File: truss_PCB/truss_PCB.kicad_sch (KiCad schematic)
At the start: 8 parts, among them J1 XT60_60A_male, J2 LimitSwitch, J3 Servo, J4 Truss Connection

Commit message: updating truss PCB
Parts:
- J3: symbol Connector:Conn_01x03_Male -> Connector:Conn_01x01_Male
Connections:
- net SERVO_GND: no longer J3.3 (Pin_3)
- net SERVO_POWER: now also J3.1 (Pin_1); no longer J3.2 (Pin_2)
- net SERVO_PWM: no longer J3.1 (Pin_1)
- net MCU/LED_1: now reaches J4.15
- net MCU/LED_3: now reaches J4.16
- net MCU/LED_2: now reaches J4.34
- net MCU/LED_4: now reaches J4.35
- no-connect marks 6 -> 2
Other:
- sheet MCU ports: added LED_1, LED_2, LED_3, LED_4; removed none
- moved on the sheet: J2, JP1, R1

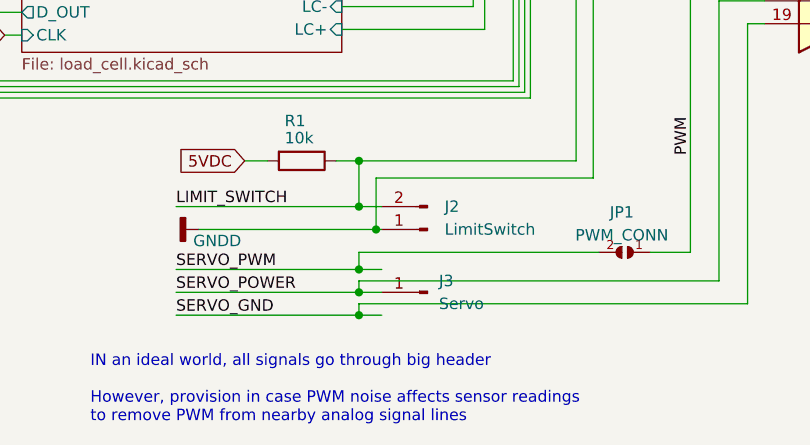
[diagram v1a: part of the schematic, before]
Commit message: Board V2 Almost Finished TODO# RUN DRC
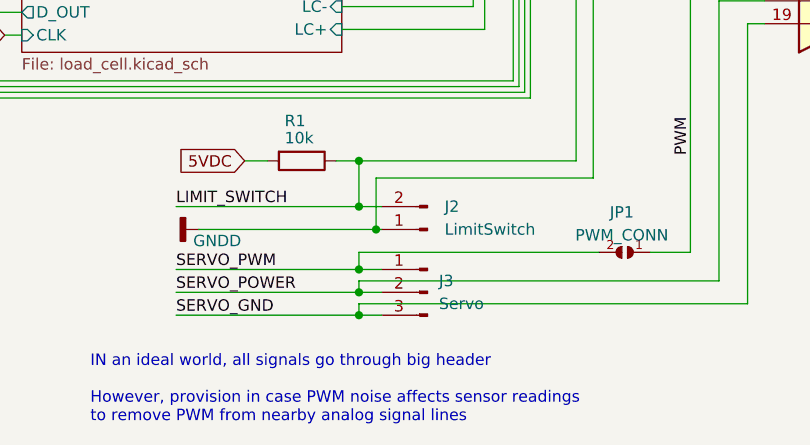
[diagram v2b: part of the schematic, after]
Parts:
- J3: symbol Connector:Conn_01x01_Male -> Connector:Conn_01x03_Male
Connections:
- net SERVO_GND: now also J3.3 (Pin_3)
- net SERVO_POWER: now also J3.2 (Pin_2); no longer J3.1 (Pin_1)
- net SERVO_PWM: now also J3.1 (Pin_1)
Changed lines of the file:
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@@
     (pin "1")
   )
-  (symbol (lib_id "Connector:Conn_01x01_Male") (at 231.14 162.56 0) (mirror y) (unit 1)
+  (symbol (lib_id "Connector:Conn_01x03_Male") (at 231.14 162.56 0) (mirror y) (unit 1)
     (in_bom yes) (on_board yes) (fields_autoplaced)
     (property "Reference" "J3" (id 0) (at 232.41 161.2899 0)
@@
       (effects (font (size 1.27 1.27)) (justify right))
     )
-    (property "Footprint" "Connector_PinHeader_2.54mm:PinHeader_1x03_P2.54mm_Vertical" (id 2) (at 231.14 162.56 0)
+    (property "Footprint" "Connector_PinHeader_2.54mm:PinHeader_1x03_P2.54mm_Vertical" (id 2) (at 227.711 169.545 0)
       (effects (font (size 1.27 1.27)) hide)
     )
@@
     )
     (pin "1")
+    (pin "2")
+    (pin "3")
   )
   (symbol (lib_id "Connector:DB37_Female_MountingHoles") (at 276.225 86.995 0) (unit 1)
@@
       (reference "D2") (unit 1) (value "BZV55B9V1") (footprint "Diode_SMD:D_MiniMELF")
     )
-    (path "/c34a27f7-e16c-48f3-87ee-04b6d0a7d0a9/1778d3a6-bace-44ff-b226-03c631eedf05"
-      (reference "D3") (unit 1) (value "12V Power") (footprint "Diode_SMD:D_0805_2012Metric_Pad1.15x1.40mm_HandSolder")
+    (path "/c34a27f7-e16c-48f3-87ee-04b6d0a7d0a9/4c37b896-33bd-4871-8fb1-55f67478f1bc"
+      (reference "D3") (unit 1) (value "3v3 MCU Power (blu)") (footprint "Diode_SMD:D_0805_2012Metric_Pad1.15x1.40mm_HandSolder")
     )
     (path "/c34a27f7-e16c-48f3-87ee-04b6d0a7d0a9/a76338dd-38ac-4367-b51a-19c6e020da56"
       (reference "D4") (unit 1) (value "1N5821") (footprint "Diode_SMD:D_SMA")
     )
-    (path "/c34a27f7-e16c-48f3-87ee-04b6d0a7d0a9/6836696c-7a6e-4837-b2ca-003ce78f3a71"
-      (reference "D5") (unit 1) (value "6v Servo Power") (footprint "Diode_SMD:D_0805_2012Metric_Pad1.15x1.40mm_HandSolder")
-    )
-    (path "/c34a27f7-e16c-48f3-87ee-04b6d0a7d0a9/b0d97af1-709c-4944-ab52-2f8634855238"
-      (reference "D6") (unit 1) (value "10V Power") (footprint "Diode_SMD:D_0805_2012Metric_Pad1.15x1.40mm_HandSolder")
-    )
-    (path "/c34a27f7-e16c-48f3-87ee-04b6d0a7d0a9/4d57fa7d-1b13-4e9d-9e55-e3a5cb57dad7"
-      (reference "D7") (unit 1) (value "5v MCU Power") (footprint "Diode_SMD:D_0805_2012Metric_Pad1.15x1.40mm_HandSolder")
-    )
-    (path "/c34a27f7-e16c-48f3-87ee-04b6d0a7d0a9/97f4cb04-730f-4dba-b564-05ca06b23805"
-      (reference "D8") (unit 1) (value "3v3 MCU Power") (footprint "Diode_SMD:D_0805_2012Metric_Pad1.15x1.40mm_HandSolder")
+    (path "/c34a27f7-e16c-48f3-87ee-04b6d0a7d0a9/60c19c44-b0f8-4c15-b1fd-f8b63483a31e"
+      (reference "D5") (unit 1) (value "6v Servo Power (grn)") (footprint "Diode_SMD:D_0805_2012Metric_Pad1.15x1.40mm_HandSolder")
+    )
+    (path "/c34a27f7-e16c-48f3-87ee-04b6d0a7d0a9/5689320f-0734-413c-a4ec-4ec0c7b735b2"
+      (reference "D6") (unit 1) (value "10V Power (orng)") (footprint "Diode_SMD:D_0805_2012Metric_Pad1.15x1.40mm_HandSolder")
+    )
+    (path "/c34a27f7-e16c-48f3-87ee-04b6d0a7d0a9/d59fa11c-7126-458e-a559-75be258dfe78"
+      (reference "D7") (unit 1) (value "5v MCU Power (yllw)") (footprint "Diode_SMD:D_0805_2012Metric_Pad1.15x1.40mm_HandSolder")
+    )
+    (path "/c34a27f7-e16c-48f3-87ee-04b6d0a7d0a9/70dff86c-3471-46b6-bc2b-9ba0f3f8fe5d"
+      (reference "D8") (unit 1) (value "12V Power (red)") (footprint "Diode_SMD:D_0805_2012Metric_Pad1.15x1.40mm_HandSolder")
     )
     (path "/ba26ee21-6561-4a71-81c1-93b0e4e983d4/4144bd5a-b19f-4bda-9741-57670c9b0841"
@@
     )
     (path "/14e50a82-f75d-4fcb-ad4e-3c36814d2442"
-      (reference "J3") (unit 1) (value "Servo") (footprint "Connector_PinHeader_2.54mm:PinHeader_1x01_P2.54mm_Vertical")
+      (reference "J3") (unit 1) (value "Servo") (footprint "Connector_PinHeader_2.54mm:PinHeader_1x03_P2.54mm_Vertical")
     )
     (path "/1ff63a68-ee92-4626-a1e8-11178b819d19"
@@
       (reference "R38") (unit 1) (value "330r") (footprint "Resistor_SMD:R_0805_2012Metric_Pad1.20x1.40mm_HandSolder")
     )
-    (path "/c34a27f7-e16c-48f3-87ee-04b6d0a7d0a9/f63dcf07-c9b4-453f-8c30-50d1f069ab0f"
-      (reference "R39") (unit 1) (value "10k") (footprint "Resistor_SMD:R_0805_2012Metric_Pad1.20x1.40mm_HandSolder")
-    )
-    (path "/c34a27f7-e16c-48f3-87ee-04b6d0a7d0a9/fa1aeb6d-fed2-4355-9cd8-0afb49942f2c"
-      (reference "R40") (unit 1) (value "1k") (footprint "Resistor_SMD:R_0805_2012Metric_Pad1.20x1.40mm_HandSolder")
-    )
-    (path "/c34a27f7-e16c-48f3-87ee-04b6d0a7d0a9/ce358d1a-0e0c-4441-8371-c0b92445399e"
+    (path "/c34a27f7-e16c-48f3-87ee-04b6d0a7d0a9/2b853e73-dfe6-4a96-bfa7-26c7b992eaa1"
+      (reference "R39") (unit 1) (value "330r") (footprint "Resistor_SMD:R_0805_2012Metric_Pad1.20x1.40mm_HandSolder")
+    )
+    (path "/c34a27f7-e16c-48f3-87ee-04b6d0a7d0a9/d74abd69-ca97-418e-9496-b64fa6d1acda"
+      (reference "R40") (unit 1) (value "10k") (footprint "Resistor_SMD:R_0805_2012Metric_Pad1.20x1.40mm_HandSolder")
+    )
+    (path "/c34a27f7-e16c-48f3-87ee-04b6d0a7d0a9/19193437-c06a-480c-b1cd-bc034912a3cc"
       (reference "R41") (unit 1) (value "8k2") (footprint "Resistor_SMD:R_0805_2012Metric_Pad1.20x1.40mm_HandSolder")
     )
-    (path "/c34a27f7-e16c-48f3-87ee-04b6d0a7d0a9/26ae8e9b-b802-46a4-8146-c068f053a284"
-      (reference "R42") (unit 1) (value "1k") (footprint "Resistor_SMD:R_0805_2012Metric_Pad1.20x1.40mm_HandSolder")
-    )
-    (path "/c34a27f7-e16c-48f3-87ee-04b6d0a7d0a9/22c6fac0-c8a9-47d7-8f29-c9a638824719"
-      (reference "R43") (unit 1) (value "330r") (footprint "Resistor_SMD:R_0805_2012Metric_Pad1.20x1.40mm_HandSolder")
+    (path "/c34a27f7-e16c-48f3-87ee-04b6d0a7d0a9/474dbc44-c3c3-4b6a-8dca-f455d1c9e0de"
+      (reference "R42") (unit 1) (value "8k2") (footprint "Resistor_SMD:R_0805_2012Metric_Pad1.20x1.40mm_HandSolder")
+    )
+    (path "/c34a27f7-e16c-48f3-87ee-04b6d0a7d0a9/18fd7230-9635-47aa-9d63-57ae6f48d97f"
+      (reference "R43") (unit 1) (value "1k") (footprint "Resistor_SMD:R_0805_2012Metric_Pad1.20x1.40mm_HandSolder")
     )
     (path "/ba26ee21-6561-4a71-81c1-93b0e4e983d4/4714d7f5-82e6-4cfa-b041-2201f6400764"
